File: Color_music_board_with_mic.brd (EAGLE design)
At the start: 42.9 x 66 mm, 15 parts

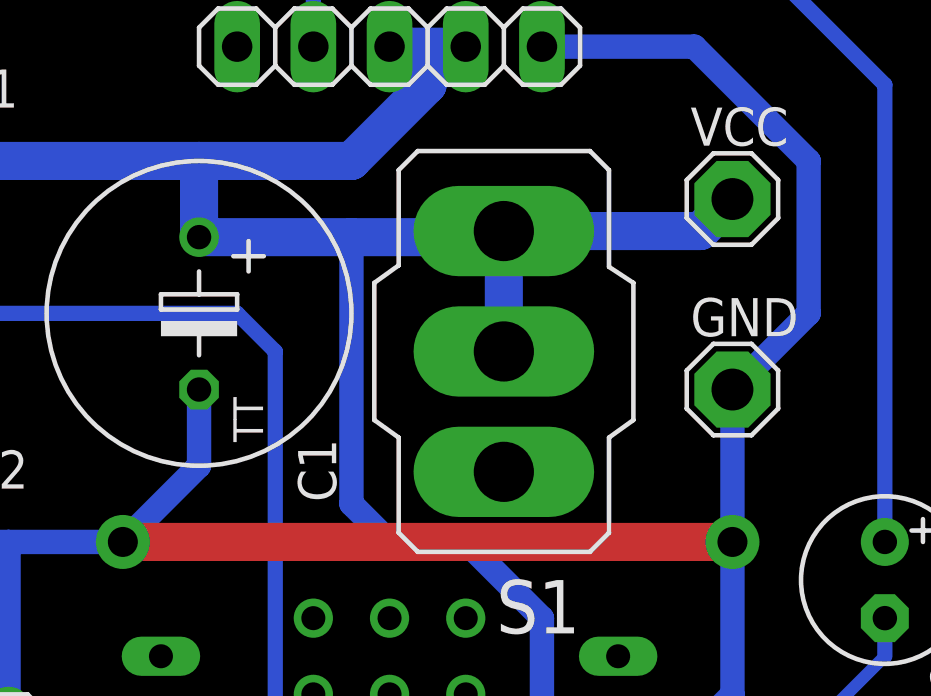
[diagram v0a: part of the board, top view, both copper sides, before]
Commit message: Fixed switch on the power line. Added a template for printing
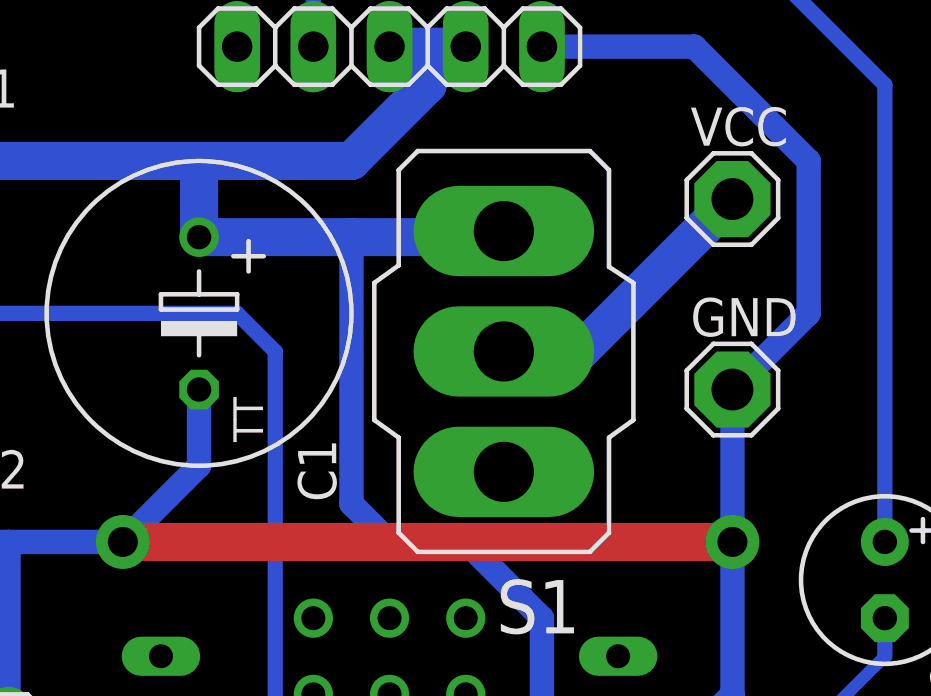
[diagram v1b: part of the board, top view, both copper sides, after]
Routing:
- net VCC: track 96.2 -> 93.5 mm
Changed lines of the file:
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@@
 <layer number="114" name="FRNTMAAT1" color="7" fill="1" visible="yes" active="yes"/>
 <layer number="115" name="FRNTMAAT2" color="7" fill="1" visible="yes" active="yes"/>
-<layer number="116" name="Patch_BOT" color="7" fill="1" visible="yes" active="yes"/>
+<layer number="116" name="centerDrill" color="7" fill="1" visible="yes" active="yes"/>
 <layer number="117" name="BACKMAAT1" color="7" fill="1" visible="yes" active="yes"/>
 <layer number="118" name="Rect_Pads" color="7" fill="1" visible="yes" active="yes"/>
@@
 <dimension x1="0" y1="66.03" x2="42.85" y2="66.03" x3="21.425" y3="72.39" textsize="1.778" layer="43"/>
 <dimension x1="43.18" y1="0" x2="43.18" y2="66.04" x3="52.07" y3="33.02" textsize="1.778" layer="43"/>
+<circle x="3.81" y="3.81" radius="1.025" width="1.55" layer="116"/>
+<circle x="3.81" y="62.23" radius="1.025" width="1.55" layer="116"/>
+<circle x="39.37" y="62.23" radius="1.025" width="1.55" layer="116"/>
+<circle x="39.37" y="3.81" radius="1.025" width="1.55" layer="116"/>
+<circle x="15.24" y="52.07" radius="0.353" width="0.206" layer="116"/>
+<circle x="15.24" y="46.99" radius="0.353" width="0.206" layer="116"/>
+<circle x="38.1" y="41.91" radius="0.353" width="0.206" layer="116"/>
+<circle x="38.1" y="39.37" radius="0.353" width="0.206" layer="116"/>
+<circle x="33.02" y="33.02" radius="0.353" width="0.206" layer="116"/>
+<circle x="35.56" y="33.02" radius="0.353" width="0.206" layer="116"/>
+<circle x="6.35" y="48.26" radius="0.499" width="0.498" layer="116"/>
+<circle x="33.02" y="46.99" radius="0.499" width="0.498" layer="116"/>
+<circle x="6.35" y="41.91" radius="0.499" width="0.498" layer="116"/>
+<circle x="16.51" y="58.42" radius="0.404" width="0.308" layer="116"/>
+<circle x="19.05" y="58.42" radius="0.404" width="0.308" layer="116"/>
+<circle x="21.59" y="58.42" radius="0.404" width="0.308" layer="116"/>
+<circle x="24.13" y="58.42" radius="0.404" width="0.308" layer="116"/>
+<circle x="26.67" y="58.42" radius="0.404" width="0.308" layer="116"/>
+<circle x="3.81" y="35.56" radius="0.404" width="0.308" layer="116"/>
+<circle x="6.35" y="35.56" radius="0.404" width="0.308" layer="116"/>
+<circle x="8.89" y="35.56" radius="0.404" width="0.308" layer="116"/>
+<circle x="39.37" y="33.02" radius="0.404" width="0.308" layer="116"/>
+<circle x="39.37" y="30.48" radius="0.404" width="0.308" layer="116"/>
+<circle x="39.37" y="27.94" radius="0.404" width="0.308" layer="116"/>
+<circle x="39.37" y="25.4" radius="0.404" width="0.308" layer="116"/>
+<circle x="39.37" y="22.86" radius="0.404" width="0.308" layer="116"/>
+<circle x="19.05" y="7.62" radius="0.353" width="0.206" layer="116"/>
+<circle x="19.05" y="15.24" radius="0.353" width="0.206" layer="116"/>
+<circle x="25.4" y="44.247" radius="0.652" width="0.803" layer="116"/>
+<circle x="25.4" y="48.26" radius="0.652" width="0.803" layer="116"/>
+<circle x="25.4" y="52.273" radius="0.652" width="0.803" layer="116"/>
+<circle x="3.099" y="30.201" radius="0.404" width="0.308" layer="116"/>
+<circle x="9.601" y="30.201" radius="0.404" width="0.308" layer="116"/>
+<circle x="3.099" y="25.679" radius="0.404" width="0.308" layer="116"/>
+<circle x="9.601" y="25.679" radius="0.404" width="0.308" layer="116"/>
+<circle x="29.21" y="5.08" radius="0.35" width="0.2" layer="116"/>
+<circle x="29.21" y="30.48" radius="0.35" width="0.2" layer="116"/>
+<circle x="29.21" y="10.16" radius="0.35" width="0.2" layer="116"/>
+<circle x="29.21" y="12.7" radius="0.35" width="0.2" layer="116"/>
+<circle x="29.21" y="15.24" radius="0.35" width="0.2" layer="116"/>
+<circle x="29.21" y="17.78" radius="0.35" width="0.2" layer="116"/>
+<circle x="29.21" y="20.32" radius="0.35" width="0.2" layer="116"/>
+<circle x="29.21" y="22.86" radius="0.35" width="0.2" layer="116"/>
+<circle x="29.21" y="25.4" radius="0.35" width="0.2" layer="116"/>
+<circle x="29.21" y="27.94" radius="0.35" width="0.2" layer="116"/>
+<circle x="29.21" y="7.62" radius="0.35" width="0.2" layer="116"/>
+<circle x="13.97" y="27.94" radius="0.35" width="0.2" layer="116"/>
+<circle x="13.97" y="25.4" radius="0.35" width="0.2" layer="116"/>
+<circle x="13.97" y="22.86" radius="0.35" width="0.2" layer="116"/>
+<circle x="13.97" y="20.32" radius="0.35" width="0.2" layer="116"/>
+<circle x="13.97" y="17.78" radius="0.35" width="0.2" layer="116"/>
+<circle x="13.97" y="15.24" radius="0.35" width="0.2" layer="116"/>
+<circle x="13.97" y="12.7" radius="0.35" width="0.2" layer="116"/>
+<circle x="13.97" y="10.16" radius="0.35" width="0.2" layer="116"/>
+<circle x="13.97" y="7.62" radius="0.35" width="0.2" layer="116"/>
+<circle x="13.97" y="5.08" radius="0.35" width="0.2" layer="116"/>
+<circle x="13.97" y="2.54" radius="0.35" width="0.2" layer="116"/>
+<circle x="29.21" y="2.54" radius="0.35" width="0.2" layer="116"/>
+<circle x="29.21" y="35.56" radius="0.35" width="0.2" layer="116"/>
+<circle x="13.97" y="30.48" radius="0.35" width="0.2" layer="116"/>
+<circle x="24.13" y="39.37" radius="0.35" width="0.2" layer="116"/>
+<circle x="24.13" y="36.83" radius="0.35" width="0.2" layer="116"/>
+<circle x="21.59" y="39.37" radius="0.35" width="0.2" layer="116"/>
+<circle x="21.59" y="36.83" radius="0.35" width="0.2" layer="116"/>
+<circle x="19.05" y="39.37" radius="0.35" width="0.2" layer="116"/>
+<circle x="19.05" y="36.83" radius="0.35" width="0.2" layer="116"/>
+<circle x="29.21" y="38.1" radius="0.35" width="0.2" layer="116"/>
+<circle x="29.21" y="33.02" radius="0.35" width="0.2" layer="116"/>
+<circle x="13.97" y="33.02" radius="0.35" width="0.2" layer="116"/>
+<circle x="13.97" y="35.56" radius="0.35" width="0.2" layer="116"/>
+<circle x="13.97" y="38.1" radius="0.35" width="0.2" layer="116"/>
+<circle x="33.02" y="53.34" radius="0.499" width="0.498" layer="116"/>
+<circle x="6.35" y="54.61" radius="0.499" width="0.498" layer="116"/>
+<circle x="12.7" y="41.91" radius="0.4" width="0.3" layer="116"/>
+<circle x="33.02" y="41.91" radius="0.4" width="0.3" layer="116"/>
 </plain>
 <attributes>
@@
 <contactref element="VCC" pad="MP"/>
 <contactref element="S1" pad="3"/>
-<wire x1="33.02" y1="53.34" x2="31.9532" y2="52.2732" width="1.27" layer="16"/>
-<wire x1="31.9532" y1="52.2732" x2="25.4" y2="52.2732" width="1.27" layer="16"/>
-<wire x1="25.1968" y1="52.07" x2="25.4" y2="52.2732" width="1.27" layer="16"/>
 <wire x1="6.35" y1="54.61" x2="7.62" y2="54.61" width="1.27" layer="16"/>
-<wire x1="15.24" y1="52.07" x2="20.32" y2="52.07" width="1.27" layer="16"/>
 <contactref element="MIC1" pad="1"/>
-<wire x1="20.32" y1="52.07" x2="25.1968" y2="52.07" width="1.27" layer="16"/>
 <wire x1="2.54" y1="40.64" x2="2.54" y2="50.8" width="0.8128" layer="16"/>
 <contactref element="U$1" pad="5V"/>
@@
 <wire x1="15.24" y1="54.61" x2="6.35" y2="54.61" width="1.27" layer="16"/>
 <wire x1="15.24" y1="52.07" x2="15.24" y2="54.61" width="1.27" layer="16"/>
-<wire x1="20.32" y1="43.18" x2="20.32" y2="52.07" width="0.8128" layer="16"/>
-<wire x1="25.4" y1="48.26" x2="25.4" y2="52.2732" width="1.27" layer="16"/>
+<wire x1="20.32" y1="52.07" x2="20.32" y2="43.18" width="0.8128" layer="16"/>
 <wire x1="3.81" y1="35.56" x2="3.81" y2="39.37" width="0.8128" layer="16"/>
 <wire x1="3.81" y1="39.37" x2="2.54" y2="40.64" width="0.8128" layer="16"/>
+<wire x1="25.4" y1="48.26" x2="27.94" y2="48.26" width="1.27" layer="16"/>
+<wire x1="27.94" y1="48.26" x2="33.02" y2="53.34" width="1.27" layer="16"/>
+<wire x1="25.1968" y1="52.07" x2="20.32" y2="52.07" width="1.27" layer="16"/>
+<wire x1="20.32" y1="52.07" x2="15.24" y2="52.07" width="1.27" layer="16"/>
+<wire x1="25.1968" y1="52.07" x2="25.4" y2="52.2732" width="0" layer="19" extent="16-16"/>
+<wire x1="25.4" y1="48.26" x2="25.1968" y2="52.07" width="0" layer="19" extent="16-16"/>
 </signal>
 <signal name="N$3">
